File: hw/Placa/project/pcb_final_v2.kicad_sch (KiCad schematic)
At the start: 26 parts, among them J1 pin_socket-bluepill, J10 tcrt5000_conector_2, J11 tcrt5000_conector_3, J12 tcrt5000_conector_1, J2 pin_socket-bluepill, J9 tof-connector_3, SW2 key, U1 YAAJ_BluePill, U2 Receptor IR, U4 AMS1117-3.3

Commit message: pcb finalizada
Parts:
- added C1: 4,7uF, Capacitor_SMD:C_0805_2012Metric_Pad1.18x1.45mm_HandSolder, symbol Device:C_Polarized
- added C4: 100nF, Capacitor_SMD:C_0805_2012Metric_Pad1.18x1.45mm_HandSolder, symbol Device:C
- added R1: 100, Resistor_SMD:R_0805_2012Metric, symbol Device:R
- C2, C3: footprint Capacitor_SMD:C_0805_2012Metric -> Capacitor_SMD:C_0805_2012Metric_Pad1.18x1.45mm_HandSolder
- SW2: footprint Button_Switch_THT:SW_DIP_SPSTx01_Slide_6.7x4.1mm_W7.62mm_P2.54mm_LowProfile -> Button_Switch_THT:SW_CK_JS202011CQN_DPDT_Straight
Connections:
- net +3V3: now also R1.1; no longer U2.2 (Vs)
- net GNDS: now also C1.2, C4.1
- new net: C1.1, C4.2, R1.2, U2.2 (Vs)
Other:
- moved on the sheet: U2

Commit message: receptor IR no 5V
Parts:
- removed C4: 100nF, Capacitor_SMD:C_0805_2012Metric_Pad1.18x1.45mm_HandSolder, symbol Device:C
- added R2: 10k ohm, Resistor_SMD:R_0805_2012Metric, symbol Device:R
- R1: value 100 -> 330 ohm
- power_drive1: footprint TerminalBlock_Phoenix:TerminalBlock_Phoenix_MKDS-1,5-2-5.08_1x02_P5.08mm_Horizontal -> (none)
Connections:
- net +3V3: no longer R1.1
- net +5V: now also R1.1
- net +7.4V: now also power_drive1.2 (Pin_2); no longer power_drive1.1 (Pin_1)
- net D1: now also U2.1 (OUT), R2.2; no longer J12.2 (Pin_2)
- net D2: now also J12.2 (Pin_2); no longer J10.2 (Pin_2)
- net D3: now also J10.2 (Pin_2); no longer J11.2 (Pin_2)
- net D4: now also J11.2 (Pin_2); no longer U2.1 (OUT)
- net GNDPWR: now also 7.4V1.1 (Pin_1), power_drive1.1 (Pin_1); no longer 7.4V1.2 (Pin_2), power_drive1.2 (Pin_2)
- net at C1.1, R1.2, U2.2 (Vs): now also R2.1
- net at D1.2 (A): now also 7.4V1.2 (Pin_2); no longer 7.4V1.1 (Pin_1)
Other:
- moved on the sheet: 7.4V1, C1, C3, J10, J11, J12, J9, R1, U2, U4, tof-connector_1, tof-connector_2

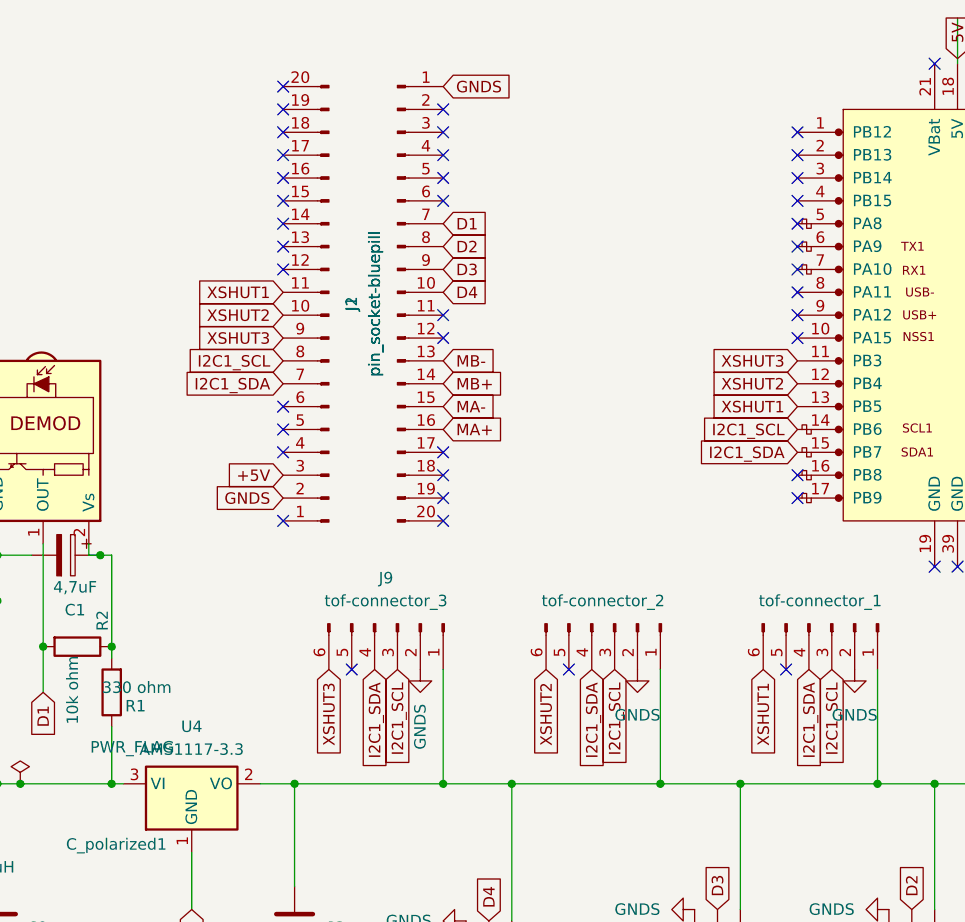
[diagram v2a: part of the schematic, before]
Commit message: adiçao dos pinos GPIO
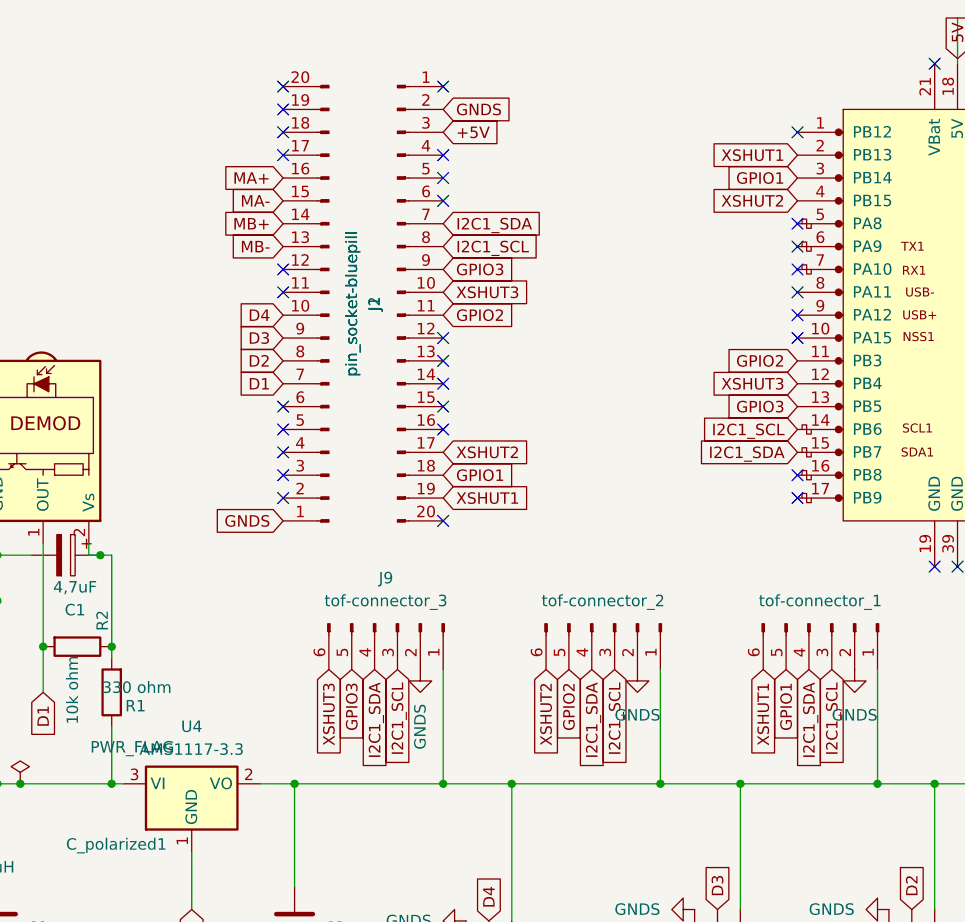
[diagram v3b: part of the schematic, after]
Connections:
- net XSHUT1: now also J2.19 (Pin_19), U1.2 (PB13); no longer J2.11 (Pin_11), U1.13 (PB5)
- net XSHUT2: now also J2.17 (Pin_17), U1.4 (PB15); no longer J2.10 (Pin_10), U1.12 (PB4)
- net XSHUT3: now also J2.10 (Pin_10), U1.12 (PB4); no longer J2.9 (Pin_9), U1.11 (PB3)
- net GPIO1: now reaches tof-connector_1.5 (Pin_5)
- net GPIO1: now also J2.18 (Pin_18), U1.3 (PB14)
- net GPIO2: now reaches tof-connector_2.5 (Pin_5)
- net GPIO2: now also J2.11 (Pin_11), U1.11 (PB3)
- net GPIO3: now reaches J9.5 (Pin_5)
- net GPIO3: now also J2.9 (Pin_9), U1.13 (PB5)
- no-connect marks 55 -> 46
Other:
- moved on the sheet: J1, J2
